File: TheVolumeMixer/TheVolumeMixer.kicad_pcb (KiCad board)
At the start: 2 copper layers, 75 x 59 mm, 58 parts, among them J1 Conn_01x01_Male, J10 Conn_01x01_Male, J2 Conn_01x01_Male, J3 Conn_01x05, J4 Conn_01x01_Male, J5 Conn_01x01_Male, J6 Conn_01x01_Male, J7 Conn_01x01_Male, J8 SJ1-3544, J9 Conn_01x01_Male, SW1 SW_Push, U1 TLC5947RHB, U2 ATSAMD21G18A-A, U3 AP2127K-3.3, U4 TPA2017, Y1 32.768kHz

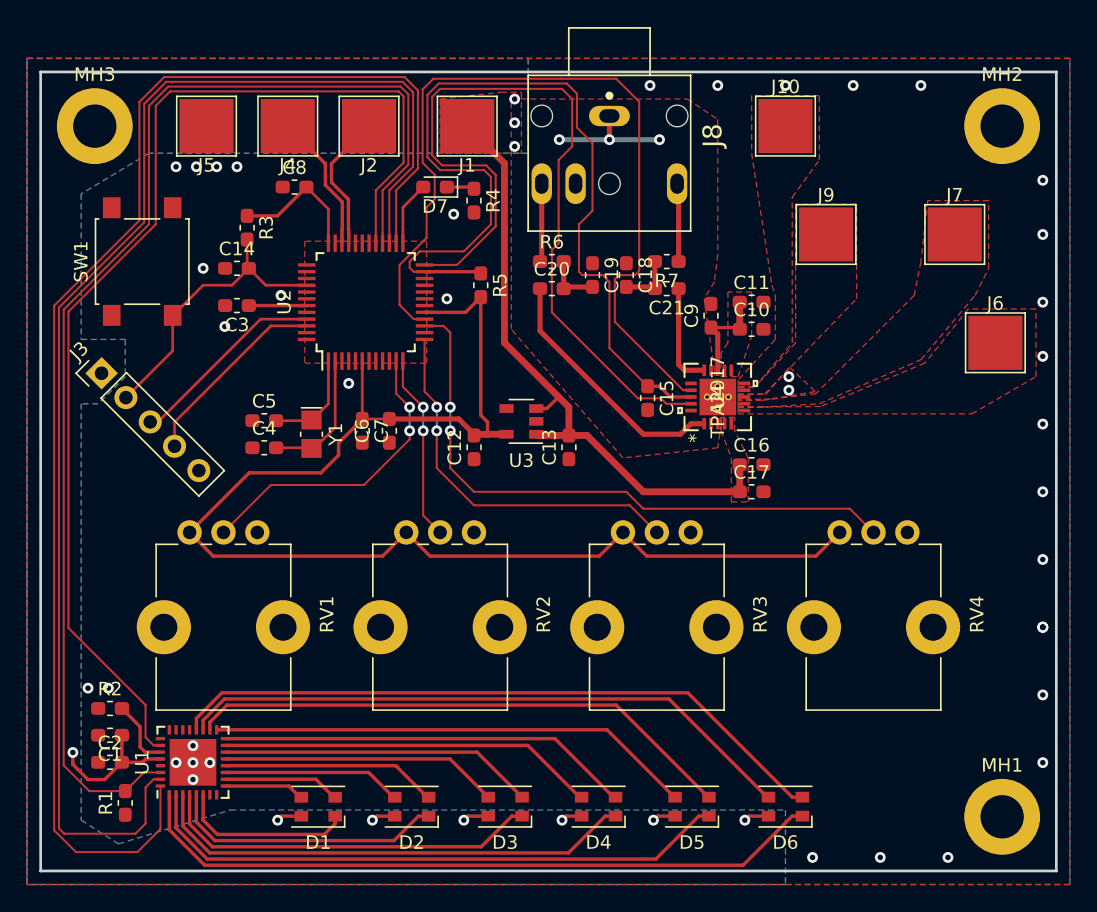
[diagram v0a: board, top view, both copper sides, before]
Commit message: fixed power traces for music amp, added all 3D models
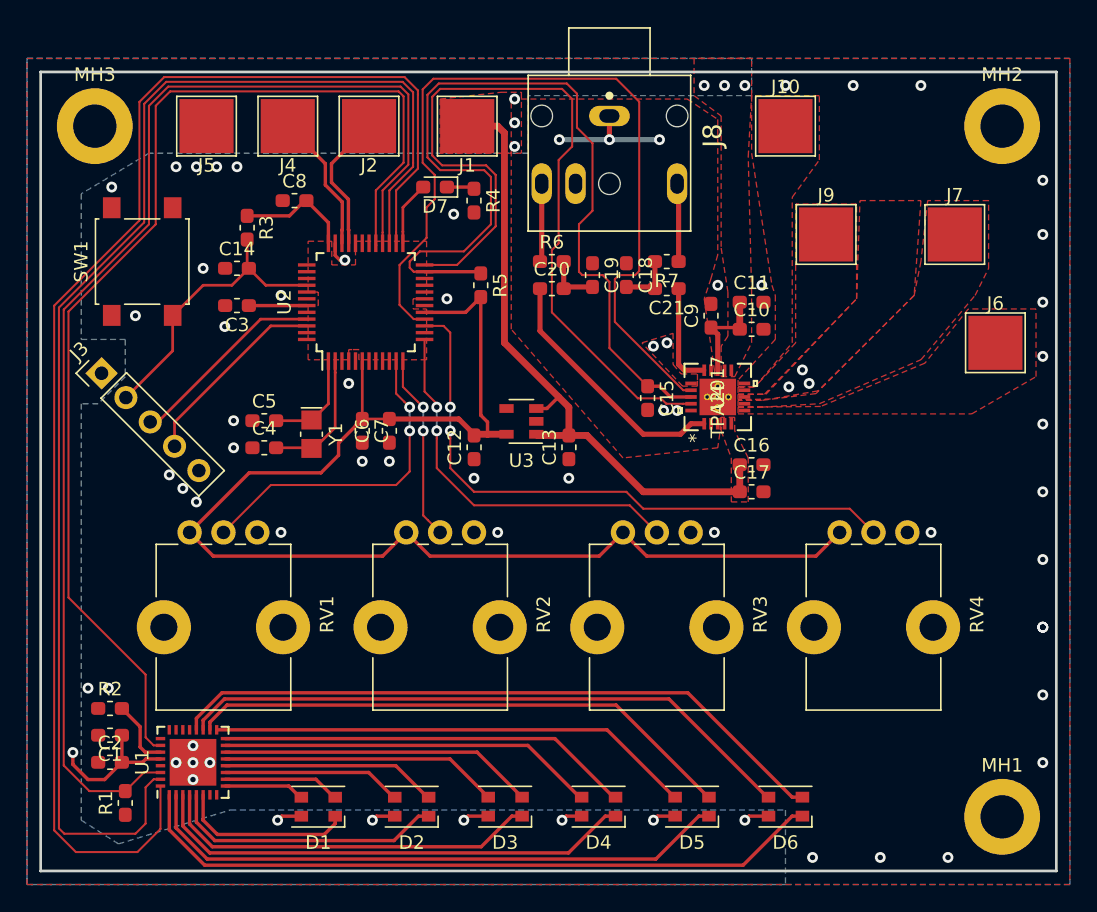
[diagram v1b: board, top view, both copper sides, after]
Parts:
- moved C8 1.00 mm to (130.8, 76.5)
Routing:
- net GND: track 0.00 -> 1.76 mm, vias 39 -> 60
- net +3V3: track 109.8 -> 108.4 mm
- net /VOL1: track 22.8 -> 24.2 mm
- net +5V: track 75.5 -> 76.8 mm, vias 10 -> 13

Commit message: updated Notes and made PCB updates
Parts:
- moved SW1 47.7 mm to (167.2, 81.9), turned to 0 degrees
- moved RV4 22.1 mm to (148.9, 100.7), turned to 0 degrees
- moved RV1 17.8 mm to (134.5, 87.4), turned to 0 degrees
- moved RV3 14.9 mm to (148.9, 87.4), turned to 0 degrees
- moved J9 8.31 mm to (173.0, 71.2)
- moved J6 5.51 mm to (182.2, 81.5)
- moved RV2 4.53 mm to (134.5, 100.7), turned to 0 degrees
- moved J7 4.10 mm to (176.2, 81.5)
- moved D1 3.50 mm to (129.0, 121.3)
- moved D6 3.00 mm to (170.0, 121.2)
- moved D2 2.20 mm to (137.2, 121.3)
- moved D5 1.70 mm to (161.8, 121.2)
- moved D3 0.90 mm to (145.4, 121.2)
- moved C1 0.50 mm to (116.6, 116.0)
- moved C2 0.50 mm to (116.6, 118.0)
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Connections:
- U2 pad 16: /SP_GC1 -> Net-(U2-Pad16)
- U2 pad 30: Net-(U2-Pad30) -> /SP_GC1
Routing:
- net GNDA: track 9.15 -> 0.00 mm, vias 3 -> 2
- net /D1_R: track 12.9 -> 8.55 mm
- net /D1_G: track 8.65 -> 5.15 mm
- net /D1_B: track 5.94 -> 2.45 mm
- net /D2_R: track 20.5 -> 17.7 mm
- net /SP_GC1: track 62.1 -> 59.6 mm
- net /D6_R: track 51.9 -> 54.4 mm
- net +5V: track 76.8 -> 74.5 mm
- net /D6_G: track 49.6 -> 51.8 mm
- net /D6_B: track 46.1 -> 48.4 mm
- net /D2_G: track 16.0 -> 13.8 mm
- net /D2_B: track 13.3 -> 11.1 mm
- net +3V3: track 108.4 -> 106.6 mm
- net /D5_B: track 35.9 -> 37.6 mm
- net /D3_R: track 28.3 -> 26.9 mm
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- added copper zone on B.Cu, net GNDA

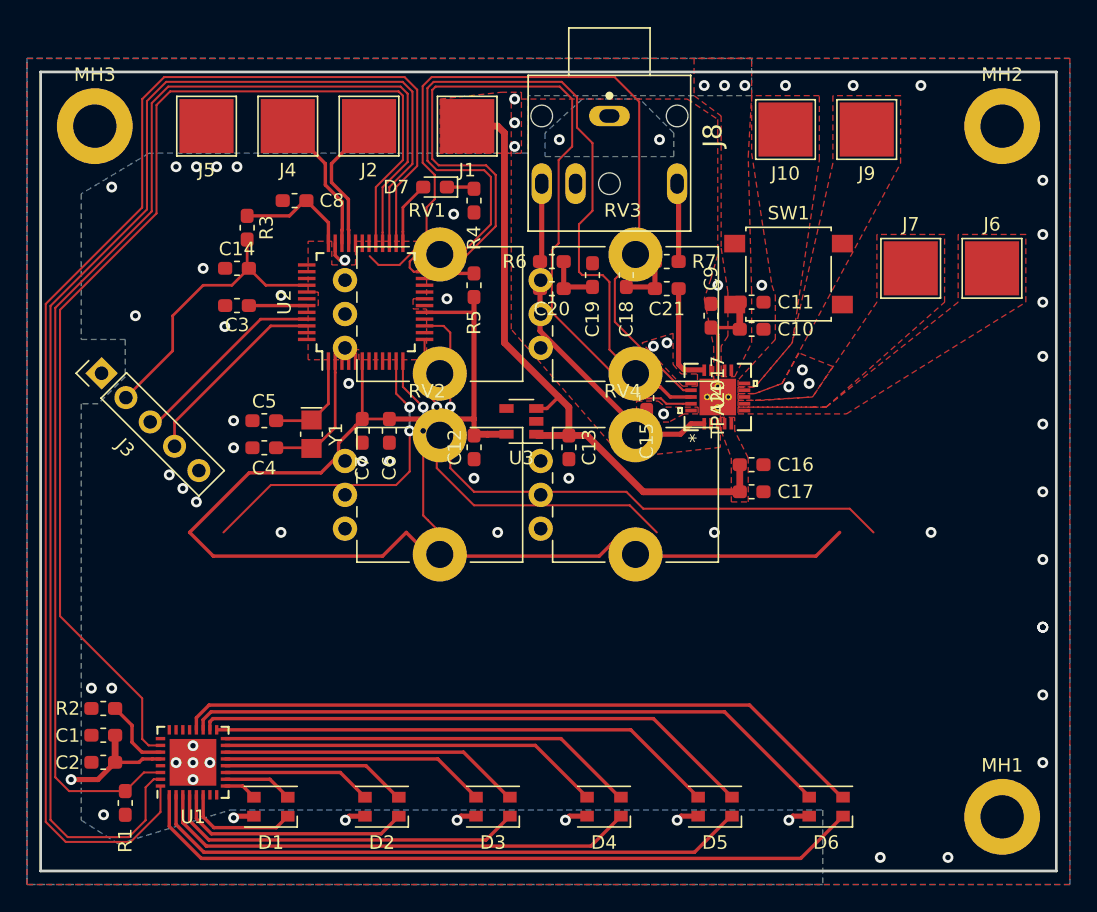
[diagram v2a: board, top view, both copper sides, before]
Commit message: PCB finished, BOM created, file system reorganized
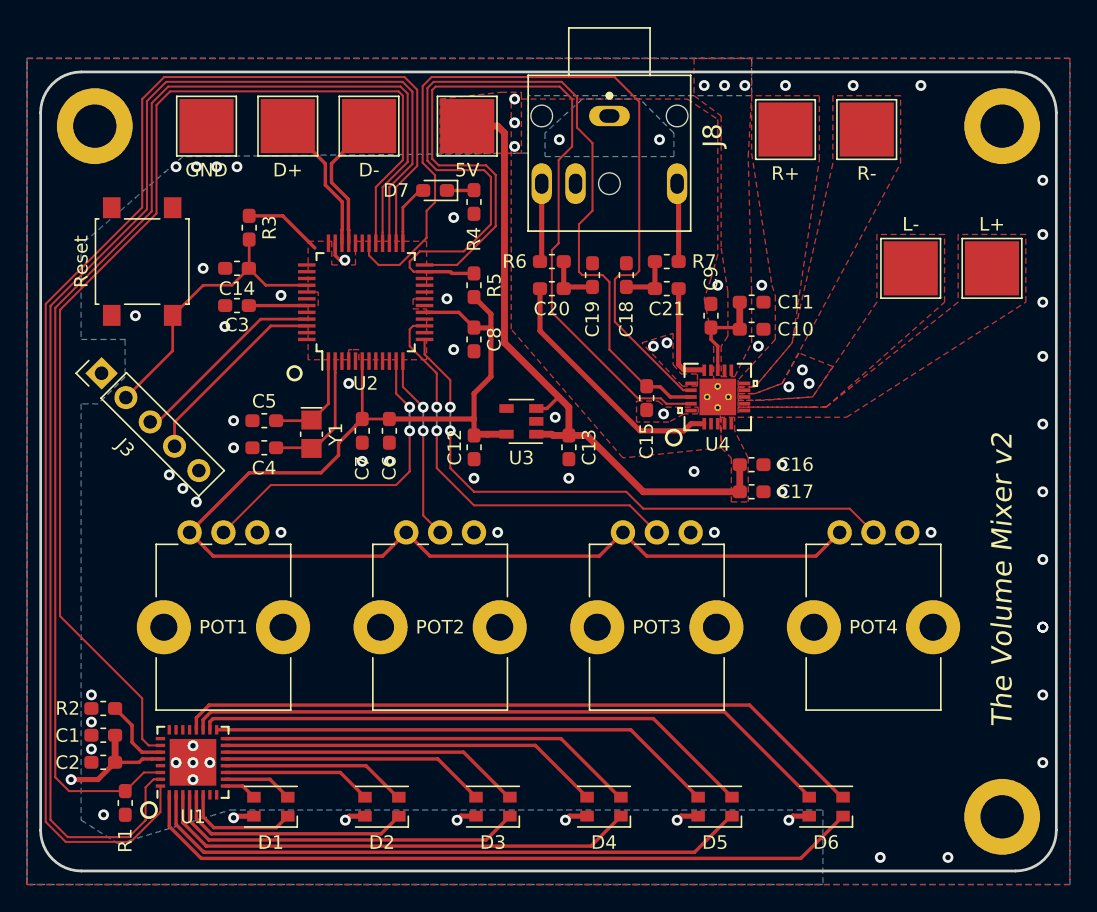
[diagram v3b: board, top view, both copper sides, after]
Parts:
- removed RV1, RV2, RV3, RV4: R_POT_US, Potentiometer - PTV09A-4020F-B203:Potentiometer_Bourns_PTV09A-1_Single_Vertical
- removed SW1: SW_Push, Button_Switch_SMD:SW_SPST_B3S-1000
- added POT1: R_POT_US, Potentiometer - PTV09A-4020F-B203:Potentiometer_Bourns_PTV09A-1_Single_Vertical, F.Cu at (123.0, 101.0)
- added POT2: R_POT_US, Potentiometer - PTV09A-4020F-B203:Potentiometer_Bourns_PTV09A-1_Single_Vertical, F.Cu at (139.0, 101.0)
- added POT3: R_POT_US, Potentiometer - PTV09A-4020F-B203:Potentiometer_Bourns_PTV09A-1_Single_Vertical, F.Cu at (155.0, 101.0)
- added POT4: R_POT_US, Potentiometer - PTV09A-4020F-B203:Potentiometer_Bourns_PTV09A-1_Single_Vertical, F.Cu at (171.0, 101.0)
- added Reset: SW_Push, Button_Switch_SMD:SW_SPST_B3S-1000, F.Cu at (119.5, 81.0)
- U4: value TPA2017 -> (none)
- moved C8 16.8 mm to (144.0, 86.8), turned to 90 degrees
- moved D7 0.25 mm to (141.1, 75.8)
- moved R3 0.15 mm to (127.4, 78.5)
- moved R4 0.10 mm to (144.0, 76.6)
- renumbered J1 to 5V, J4 to D+, J2 to D-, J5 to GND, J6 to L+, J7 to L-, J10 to R+, J9 to R-
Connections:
- U2 pad 13: /VOL3 -> /VOL4
- U2 pad 15: /VOL4 -> /VOL3
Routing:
- net /VOL3: track 28.1 -> 30.5 mm
- net /VOL4: track 45.3 -> 43.5 mm
- net /SP_GC1: track 59.6 -> 60.5 mm
- net GND: vias 59 -> 65
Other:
- outline, holes or cut-outs redrawn
- board text added: "POT1"
- board text added: "POT2"
- board text added: "POT3"
- board text added: "POT4"
- board text added: "The Volume Mixer v2"
